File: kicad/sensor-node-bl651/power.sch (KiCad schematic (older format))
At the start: 10 parts, among them P1 TPS61098x, U2 DMP2008UFG-7

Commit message: apply finishing touches
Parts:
- L1: value 4.7µF -> 4.7µH; footprint Capacitor_SMD:C_0603_1608Metric -> Inductor_SMD:L_1008_2520Metric; Description (none) -> FIXED IND 4.7UH 950MA 300 MOHM; Digi-Key Part Number (none) -> 445-174072-1-ND; Manufacturer (none) -> TDK Corporation; Manufacturer Part Number (none) -> VLF252010MT-4R7M-CA
- P1: Digi-Key Part Number 296-43747-1-ND -> 296-48759-6-ND; Manufacturer Part Number TPS610985DSET -> TPS61098DSE
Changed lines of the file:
@@
 F 2 "HH_TexasInstruments:TPS61098x" H 7350 3500 50  0001 C CNN
 F 3 "http://www.ti.com/general/docs/suppproductinfo.tsp?distId=10&gotoUrl=http%3A%2F%2Fwww.ti.com%2Flit%2Fgpn%2Ftps610985" H 7350 3500 50  0001 C CNN
-F 4 "296-43747-1-ND" H 7350 3500 50  0001 C CNN "Digi-Key Part Number"
+F 4 "296-48759-6-ND" H 7350 3500 50  0001 C CNN "Digi-Key Part Number"
 F 5 "Texas Instruments" H 7350 3500 50  0001 C CNN "Manufacturer"
-F 6 "TPS610985DSET" H 7350 3500 50  0001 C CNN "Manufacturer Part Number"
+F 6 "TPS61098DSE" H 7350 3500 50  0001 C CNN "Manufacturer Part Number"
 F 7 "IC REG DL BOOST/LNR SYNC 6WSON" H 7350 3500 50  0001 C CNN "Description"
 	1    7350 3500
@@
 P 6350 3350
 F 0 "L1" V 6540 3350 50  0000 C CNN
-F 1 "4.7µF" V 6449 3350 50  0000 C CNN
-F 2 "Capacitor_SMD:C_0603_1608Metric" H 6350 3350 50  0001 C CNN
-F 3 "~" H 6350 3350 50  0001 C CNN
+F 1 "4.7µH" V 6449 3350 50  0000 C CNN
+F 2 "Inductor_SMD:L_1008_2520Metric" H 6350 3350 50  0001 C CNN
+F 3 "https://media.digikey.com/pdf/Data%20Sheets/TDK%20PDFs/VLF252010MT-CA_Series.pdf" H 6350 3350 50  0001 C CNN
+F 4 "445-174072-1-ND" V 6350 3350 50  0001 C CNN "Digi-Key Part Number"
+F 5 "TDK Corporation" V 6350 3350 50  0001 C CNN "Manufacturer"
+F 6 "VLF252010MT-4R7M-CA" V 6350 3350 50  0001 C CNN "Manufacturer Part Number"
+F 7 "FIXED IND 4.7UH 950MA 300 MOHM" V 6350 3350 50  0001 C CNN "Description"
 	1    6350 3350
 	0    -1   -1   0

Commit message: remove fuses
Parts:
- removed F1: Polyfuse, Fuse:Fuse_0603_1608Metric, symbol Device:Polyfuse
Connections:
- wire segments 46 -> 45
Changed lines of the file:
@@
-$EndComp
-$Comp
-L Device:Polyfuse F1
-U 1 1 6017967B
-P 3650 4250
-F 0 "F1" V 3425 4250 50  0000 C CNN
-F 1 "Polyfuse" V 3516 4250 50  0000 C CNN
-F 2 "Fuse:Fuse_0603_1608Metric" H 3700 4050 50  0001 L CNN
-F 3 "https://belfuse.com/resources/datasheets/circuitprotection/ds-cp-0zcm-series.pdf" H 3650 4250 50  0001 C CNN
-F 4 "507-0ZCM0002FF2GCT-ND" V 3650 4250 50  0001 C CNN "Digi-Key Part Number"
-F 5 "Bel Fuse Inc." V 3650 4250 50  0001 C CNN "Manufacturer"
-F 6 "0ZCM0002FF2G" V 3650 4250 50  0001 C CNN "Manufacturer Part Number"
-F 7 "PTC RESET FUSE 60V 20MA 0603" V 3650 4250 50  0001 C CNN "Description"
-	1    3650 4250
-	0    1    1    0
 $EndComp
 $Comp
@@
 Wire Wire Line
 	3050 3350 3950 3350
-Wire Wire Line
-	3050 4250 3500 4250
-Wire Wire Line
-	3800 4250 5000 4250
 Connection ~ 5000 4250
 $Comp
@@
 Text HLabel 5000 3350 1    50   Input ~ 0
 UVLO
+Wire Wire Line
+	3050 4250 5000 4250
 $EndSCHEMATC

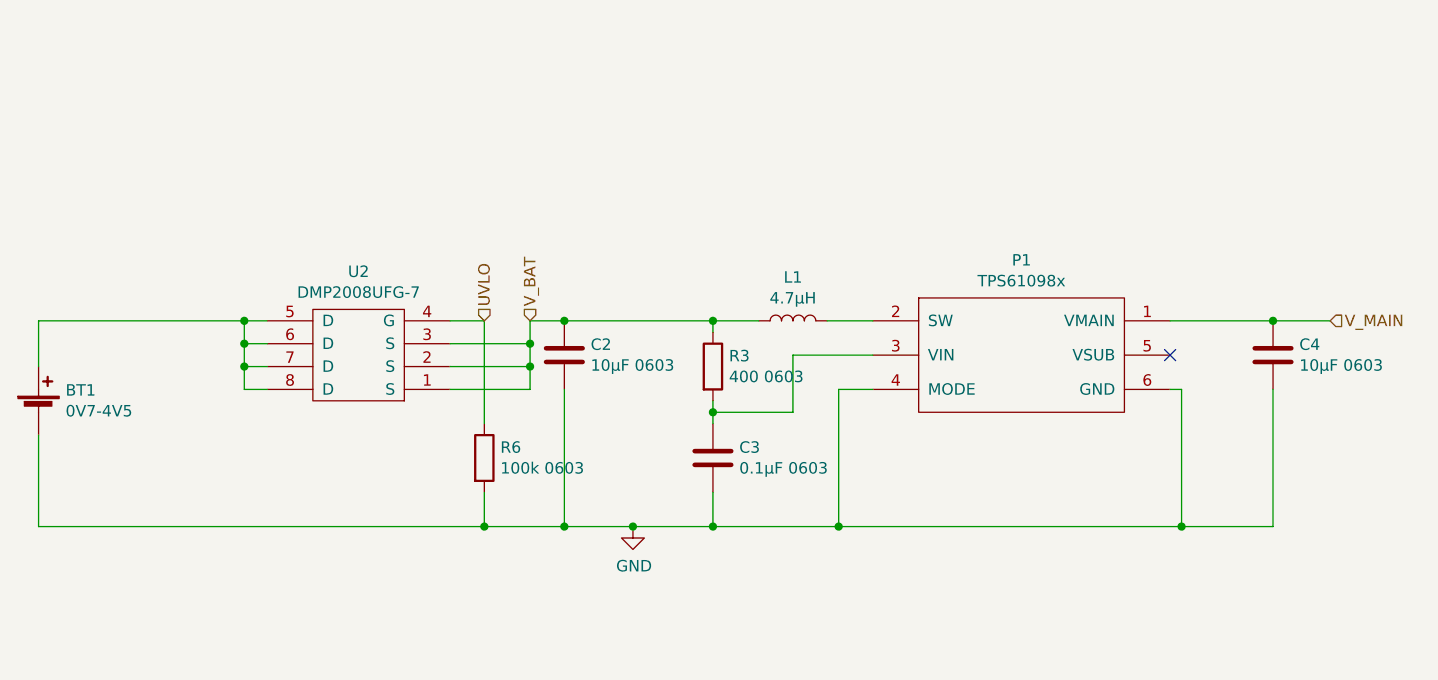
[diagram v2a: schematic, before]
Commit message: add TPS6031x
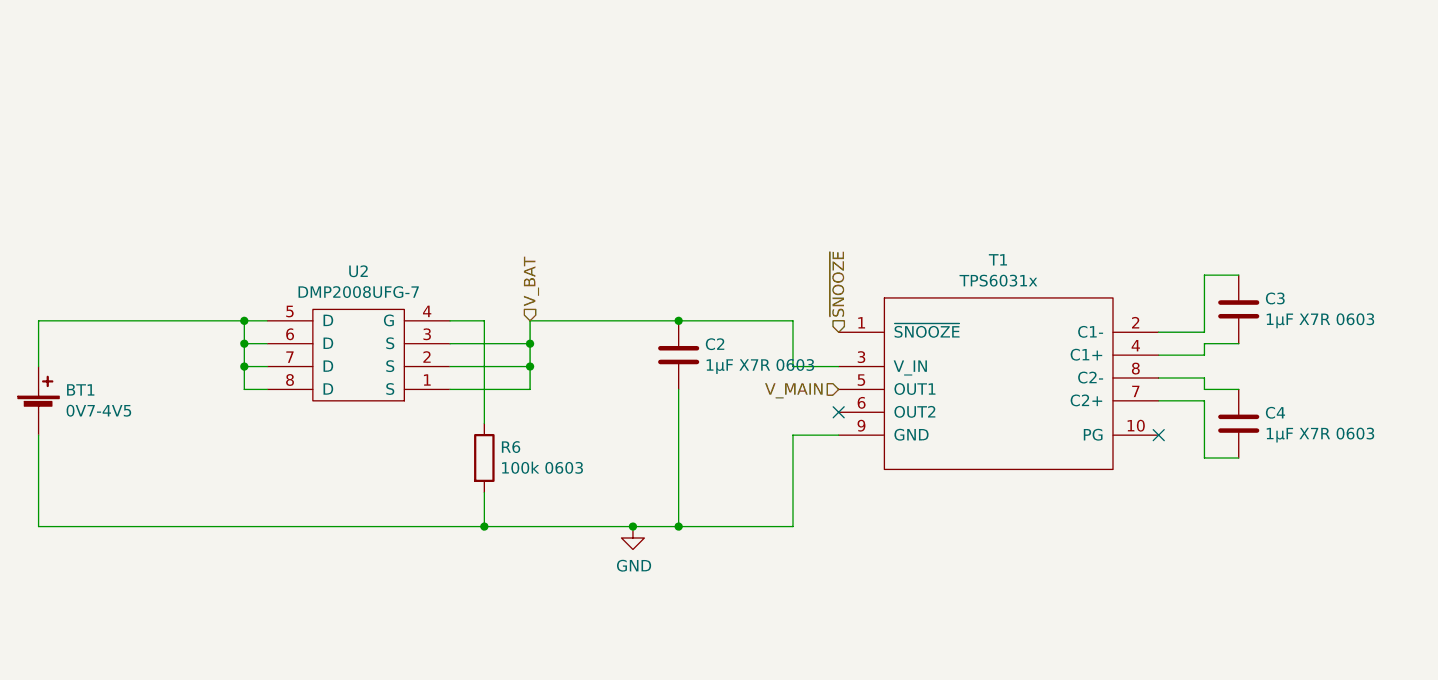
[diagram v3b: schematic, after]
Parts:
- removed L1: 4.7µH, Inductor_SMD:L_1008_2520Metric, symbol Device:L
- removed P1: TPS61098x, HH_TexasInstruments:TPS61098x, symbol HH_TexasInstruments:TPS61098x
- removed R3: 400 0603, Resistor_SMD:R_0603_1608Metric, symbol Device:R
- added T1: TPS6031x, Package_SO:MSOP-10_3x3mm_P0.5mm, symbol HH_TexasInstruments:TPS6031x
- C2, C4: value 10µF 0603 -> 1µF X7R 0603
- C3: value 0.1µF 0603 -> 1µF X7R 0603
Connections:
- net GND: now also T1.9 (GND); no longer C3.2, C4.2
- net V_BAT: now also T1.3 (V_IN)
- net V_MAIN: now also T1.5 (OUT1); no longer C4.1
- net at C3.1: now also T1.2 (C1-)
- net UVLO: no longer names the net of R6.1, U2.4 (G)
- new net: C3.2, T1.4 (C1+)
- new net: C4.2, T1.7 (C2+)
- new net: C4.1, T1.8 (C2-)
- new net ~SNOOZE: T1.1 (~SNOOZE)
- no-connect marks 1 -> 2
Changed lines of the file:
@@
 Comment4 ""
 $EndDescr
-$Comp
-L HH_TexasInstruments:TPS61098x P1
-U 1 1 6016D66E
-P 7350 3500
-F 0 "P1" H 7350 3915 50  0000 C CNN
-F 1 "TPS61098x" H 7350 3824 50  0000 C CNN
-F 2 "HH_TexasInstruments:TPS61098x" H 7350 3500 50  0001 C CNN
-F 3 "http://www.ti.com/general/docs/suppproductinfo.tsp?distId=10&gotoUrl=http%3A%2F%2Fwww.ti.com%2Flit%2Fgpn%2Ftps610985" H 7350 3500 50  0001 C CNN
-F 4 "296-48759-6-ND" H 7350 3500 50  0001 C CNN "Digi-Key Part Number"
-F 5 "Texas Instruments" H 7350 3500 50  0001 C CNN "Manufacturer"
-F 6 "TPS61098DSE" H 7350 3500 50  0001 C CNN "Manufacturer Part Number"
-F 7 "IC REG DL BOOST/LNR SYNC 6WSON" H 7350 3500 50  0001 C CNN "Description"
-	1    7350 3500
-	1    0    0    -1
-$EndComp
-$Comp
-L Device:C C2
-U 1 1 6016E335
-P 5350 3500
-F 0 "C2" H 5465 3546 50  0000 L CNN
-F 1 "10µF 0603" H 5465 3455 50  0000 L CNN
-F 2 "Capacitor_SMD:C_0603_1608Metric" H 5388 3350 50  0001 C CNN
-F 3 "~" H 5350 3500 50  0001 C CNN
-	1    5350 3500
-	1    0    0    -1
-$EndComp
-$Comp
-L Device:C C4
-U 1 1 6016E86C
-P 8450 3500
-F 0 "C4" H 8565 3546 50  0000 L CNN
-F 1 "10µF 0603" H 8565 3455 50  0000 L CNN
-F 2 "Capacitor_SMD:C_0603_1608Metric" H 8488 3350 50  0001 C CNN
-F 3 "~" H 8450 3500 50  0001 C CNN
-	1    8450 3500
-	1    0    0    -1
-$EndComp
-Text HLabel 8700 3350 2    50   Input ~ 0
+Text HLabel 6550 3650 0    50   Input ~ 0
 V_MAIN
-Connection ~ 8450 3350
-Wire Wire Line
-	8450 3350 8700 3350
-Wire Wire Line
-	8000 3650 8050 3650
-$Comp
-L Device:C C3
-U 1 1 60172574
-P 6000 3950
-F 0 "C3" H 6115 3996 50  0000 L CNN
-F 1 "0.1µF 0603" H 6115 3905 50  0000 L CNN
-F 2 "Capacitor_SMD:C_0603_1608Metric" H 6038 3800 50  0001 C CNN
-F 3 "~" H 6000 3950 50  0001 C CNN
-	1    6000 3950
-	1    0    0    -1
-$EndComp
-$Comp
-L Device:L L1
-U 1 1 60173BBD
-P 6350 3350
-F 0 "L1" V 6540 3350 50  0000 C CNN
-F 1 "4.7µH" V 6449 3350 50  0000 C CNN
-F 2 "Inductor_SMD:L_1008_2520Metric" H 6350 3350 50  0001 C CNN
-F 3 "https://media.digikey.com/pdf/Data%20Sheets/TDK%20PDFs/VLF252010MT-CA_Series.pdf" H 6350 3350 50  0001 C CNN
-F 4 "445-174072-1-ND" V 6350 3350 50  0001 C CNN "Digi-Key Part Number"
-F 5 "TDK Corporation" V 6350 3350 50  0001 C CNN "Manufacturer"
-F 6 "VLF252010MT-4R7M-CA" V 6350 3350 50  0001 C CNN "Manufacturer Part Number"
-F 7 "FIXED IND 4.7UH 950MA 300 MOHM" V 6350 3350 50  0001 C CNN "Description"
-	1    6350 3350
-	0    -1   -1   0
-$EndComp
-$Comp
-L Device:R R3
-U 1 1 601746B0
-P 6000 3550
-F 0 "R3" H 6070 3596 50  0000 L CNN
-F 1 "400 0603" H 6070 3505 50  0000 L CNN
-F 2 "Resistor_SMD:R_0603_1608Metric" V 5930 3550 50  0001 C CNN
-F 3 "~" H 6000 3550 50  0001 C CNN
-	1    6000 3550
-	1    0    0    -1
-$EndComp
-Wire Wire Line
-	5350 3350 6000 3350
-Wire Wire Line
-	6500 3350 6700 3350
-Wire Wire Line
-	6000 3350 6000 3400
-Connection ~ 6000 3350
-Wire Wire Line
-	6000 3350 6200 3350
-Wire Wire Line
-	6000 3700 6000 3750
-Wire Wire Line
-	6000 3750 6350 3750
-Wire Wire Line
-	6350 3750 6350 3500
-Wire Wire Line
-	6350 3500 6700 3500
-Connection ~ 6000 3750
-Wire Wire Line
-	6000 3750 6000 3800
 $Comp
 L power:GND #PWR02
@@
 	1    0    0    -1
 $EndComp
-Wire Wire Line
-	5650 4250 6000 4250
-Wire Wire Line
-	6000 4250 6000 4100
-Wire Wire Line
-	5650 4250 5350 4250
-Wire Wire Line
-	5350 4250 5350 3650
 Connection ~ 5650 4250
 $Comp
@@
 	5200 3650 5200 3550
 Wire Wire Line
-	5200 3350 5350 3350
-Connection ~ 5350 3350
-Wire Wire Line
 	4850 3550 5200 3550
 Connection ~ 5200 3550
@@
 Wire Wire Line
 	5000 3350 5000 3800
-Wire Wire Line
-	5000 4250 5350 4250
-Connection ~ 5350 4250
-NoConn ~ 8000 3500
-Wire Wire Line
-	8000 3350 8450 3350
 Text HLabel 5200 3350 1    50   Input ~ 0
 V_BAT
-Wire Wire Line
-	6000 4250 6550 4250
-Wire Wire Line
-	8050 3650 8050 4250
-Connection ~ 6000 4250
-Wire Wire Line
-	8050 4250 8450 4250
-Wire Wire Line
-	8450 3650 8450 4250
-Connection ~ 8050 4250
-Wire Wire Line
-	6700 3650 6550 3650
-Wire Wire Line
-	6550 3650 6550 4250
-Connection ~ 6550 4250
-Wire Wire Line
-	6550 4250 8050 4250
 Wire Wire Line
 	3050 3350 3950 3350
@@
 Wire Wire Line
 	5000 4100 5000 4250
-Text HLabel 5000 3350 1    50   Input ~ 0
-UVLO
 Wire Wire Line
 	3050 4250 5000 4250
+$Comp
+L HH_TexasInstruments:TPS6031x T1
+U 1 1 60B47905
+P 7250 3600
+F 0 "T1" H 7250 4115 50  0000 C CNN
+F 1 "TPS6031x" H 7250 4024 50  0000 C CNN
+F 2 "Package_SO:MSOP-10_3x3mm_P0.5mm" H 7250 3600 50  0001 C CNN
+F 3 "https://www.ti.com/general/docs/suppproductinfo.tsp?distId=10&gotoUrl=https%3A%2F%2Fwww.ti.com%2Flit%2Fgpn%2Ftps60310" H 7250 3600 50  0001 C CNN
+F 4 "296-13417-1-ND" H 7250 3600 50  0001 C CNN "Digi-Key Part Number"
+F 5 "Texas Instruments" H 7250 3600 50  0001 C CNN "Manufacturer"
+F 6 "TPS60313DGSR" H 7250 3600 50  0001 C CNN "Manufacturer Part Number"
+F 7 "IC REG CHRG PUMP 2VIN/3V 10VSSOP" H 7250 3600 50  0001 C CNN "Description"
+	1    7250 3600
+	1    0    0    -1
+$EndComp
+$Comp
+L Device:C C3
+U 1 1 60B48CDE
+P 8300 3300
+F 0 "C3" H 8415 3346 50  0000 L CNN
+F 1 "1µF X7R 0603" H 8415 3255 50  0000 L CNN
+F 2 "Capacitor_SMD:C_0603_1608Metric" H 8338 3150 50  0001 C CNN
+F 3 "~" H 8300 3300 50  0001 C CNN
+	1    8300 3300
+	1    0    0    -1
+$EndComp
+$Comp
+L Device:C C4
+U 1 1 60B4C1B9
+P 8300 3800
+F 0 "C4" H 8415 3846 50  0000 L CNN
+F 1 "1µF X7R 0603" H 8415 3755 50  0000 L CNN
+F 2 "Capacitor_SMD:C_0603_1608Metric" H 8338 3650 50  0001 C CNN
+F 3 "~" H 8300 3800 50  0001 C CNN
+	1    8300 3800
+	1    0    0    -1
+$EndComp
+Wire Wire Line
+	7950 3600 8150 3600
+Wire Wire Line
+	8150 3600 8150 3650
+Wire Wire Line
+	8150 3650 8300 3650
+Wire Wire Line
+	7950 3500 8150 3500
+Wire Wire Line
+	8150 3500 8150 3450
+Wire Wire Line
+	8150 3450 8300 3450
+Wire Wire Line
+	7950 3400 8150 3400
+Wire Wire Line
+	8150 3400 8150 3150
+Wire Wire Line
+	8150 3150 8300 3150
+Wire Wire Line
+	7950 3700 8150 3700
+Wire Wire Line
+	8150 3700 8150 3950
+Wire Wire Line
+	8150 3950 8300 3950
+NoConn ~ 7950 3850
+NoConn ~ 6550 3750
+Wire Wire Line
+	6550 3850 6350 3850
+Wire Wire Line
+	6350 3850 6350 4250
+Wire Wire Line
+	5650 4250 5850 4250
+Wire Wire Line
+	5000 4250 5650 4250
+Wire Wire Line
+	6350 3350 6350 3550
+Wire Wire Line
+	6350 3550 6550 3550
+Wire Wire Line
+	5850 3650 5850 4250
+Connection ~ 5850 4250
+Wire Wire Line
+	5850 4250 6350 4250
+Wire Wire Line
+	5200 3350 5850 3350
+$Comp
+L Device:C C2
+U 1 1 60B54C95
+P 5850 3500
+F 0 "C2" H 5965 3546 50  0000 L CNN
+F 1 "1µF X7R 0603" H 5965 3455 50  0000 L CNN
+F 2 "Capacitor_SMD:C_0603_1608Metric" H 5888 3350 50  0001 C CNN
+F 3 "~" H 5850 3500 50  0001 C CNN
+	1    5850 3500
+	1    0    0    -1
+$EndComp
+Connection ~ 5850 3350
+Wire Wire Line
+	5850 3350 6350 3350
+Text HLabel 6550 3400 1    50   Input ~ 0
+~SNOOZE
 $EndSCHEMATC

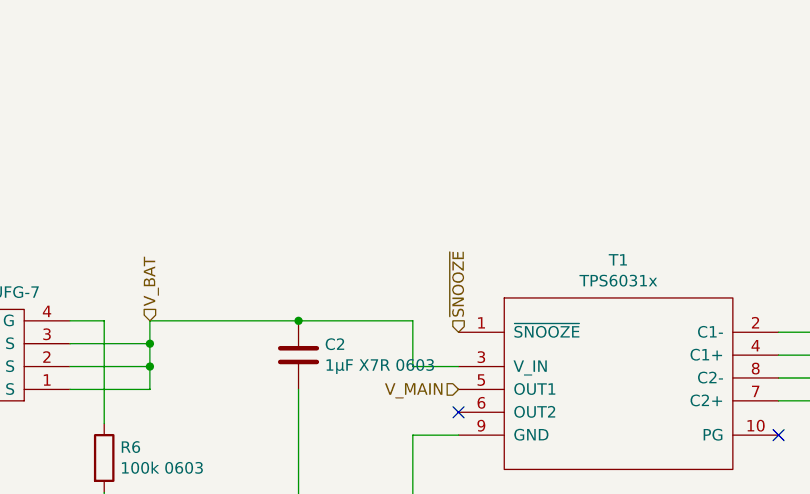
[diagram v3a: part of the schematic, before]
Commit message: add pull down on snooze line
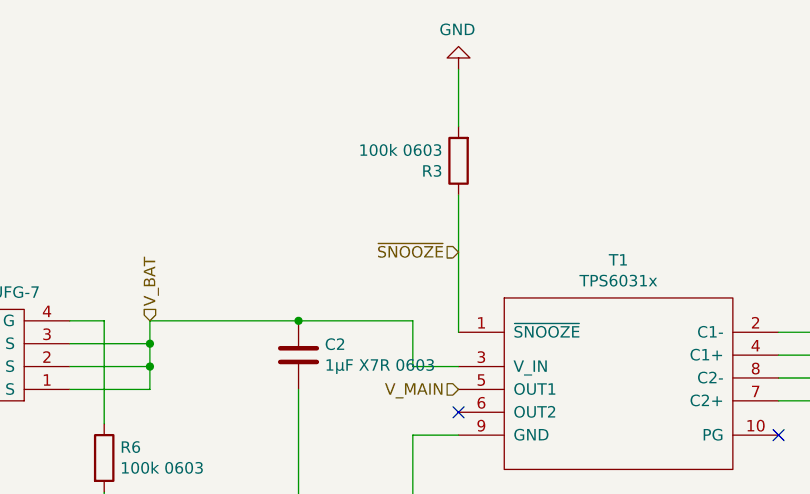
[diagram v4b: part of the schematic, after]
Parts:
- added R3: 100k 0603, Resistor_SMD:R_0603_1608Metric, symbol Device:R
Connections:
- net GND: now also R3.2
- net ~SNOOZE: now also R3.1
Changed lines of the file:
@@
 Wire Wire Line
 	5850 3350 6350 3350
-Text HLabel 6550 3400 1    50   Input ~ 0
+Text HLabel 6550 3050 0    50   Input ~ 0
 ~SNOOZE
+$Comp
+L Device:R R3
+U 1 1 60BA08BD
+P 6550 2650
+F 0 "R3" H 6620 2696 50  0000 L CNN
+F 1 "100k 0603" H 6620 2605 50  0000 L CNN
+F 2 "Resistor_SMD:R_0603_1608Metric" V 6480 2650 50  0001 C CNN
+F 3 "~" H 6550 2650 50  0001 C CNN
+	1    6550 2650
+	-1   0    0    1
+$EndComp
+Wire Wire Line
+	6550 3400 6550 2800
+$Comp
+L power:GND #PWR011
+U 1 1 60BA1E65
+P 6550 2250
+F 0 "#PWR011" H 6550 2000 50  0001 C CNN
+F 1 "GND" H 6555 2077 50  0000 C CNN
+F 2 "" H 6550 2250 50  0001 C CNN
+F 3 "" H 6550 2250 50  0001 C CNN
+	1    6550 2250
+	-1   0    0    1
+$EndComp
+Wire Wire Line
+	6550 2250 6550 2500
 $EndSCHEMATC
